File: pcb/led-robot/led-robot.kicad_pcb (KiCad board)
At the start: 2 copper layers, 29.2 x 26.2 mm, 30 parts, among them J1 data, U1 MAX7219

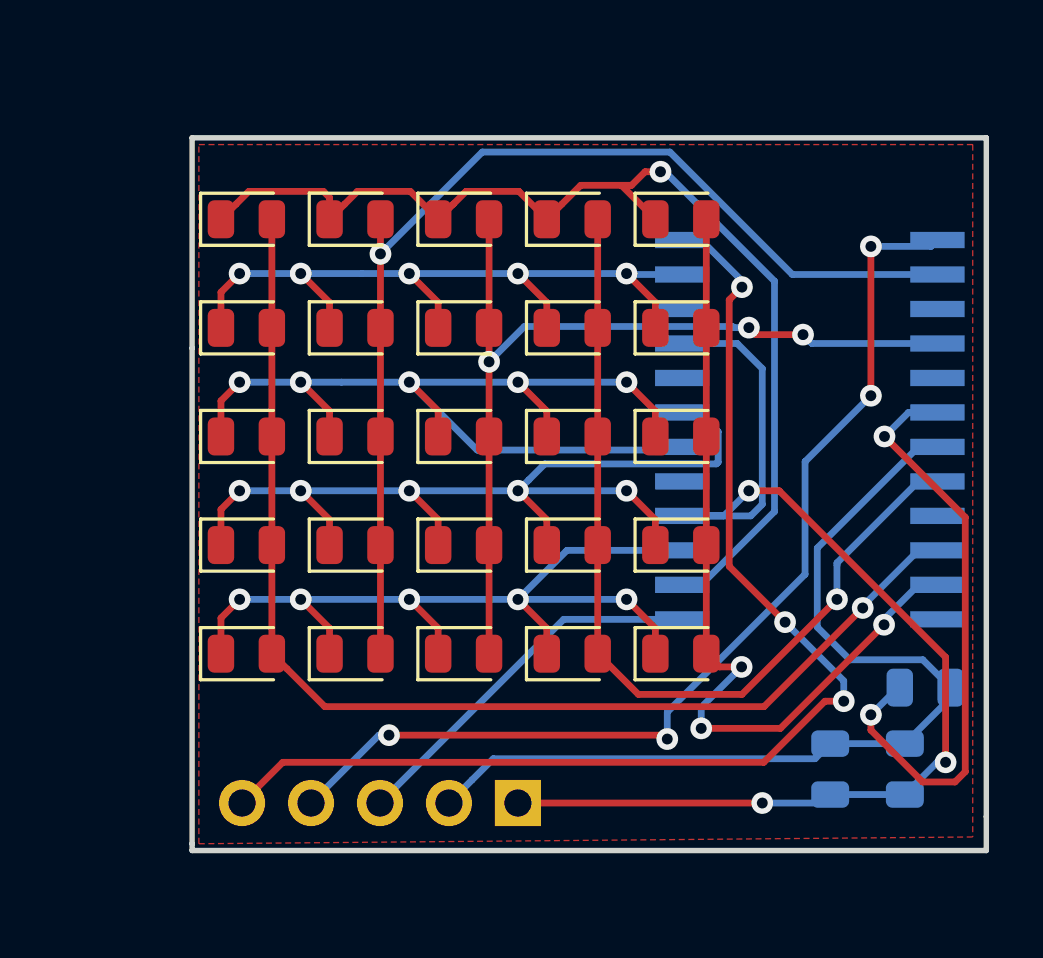
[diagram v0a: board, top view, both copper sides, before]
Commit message: update size
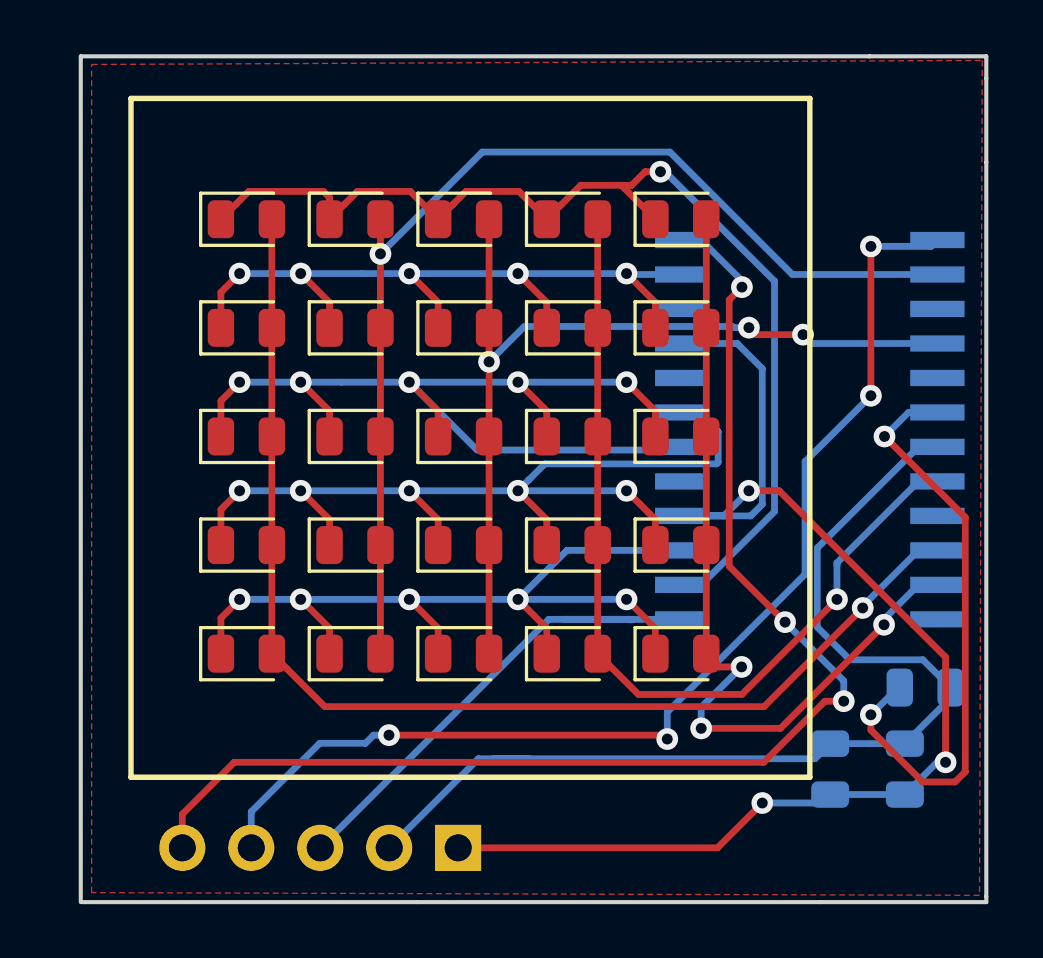
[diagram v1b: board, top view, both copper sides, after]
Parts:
- moved J1 2.75 mm to (190.8, 100.2)
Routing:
- net /DIN: track 13.9 -> 19.4 mm
- net +5V: track 35.2 -> 39.4 mm
- net /CLK: track 38.0 -> 42.0 mm
- net /LOAD: track 44.0 -> 47.6 mm
- net GND: track 44.3 -> 47.2 mm
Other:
- board size 29.2 x 26.2 mm -> 33.3 x 31.2 mm
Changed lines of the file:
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@@
   (general
     (thickness 1.6)
-    (drawings 12)
-    (tracks 247)
+    (drawings 19)
+    (tracks 256)
     (zones 0)
     (modules 30)
@@
   )
   (module Connector_PinHeader_2.54mm:PinHeader_1x05_P2.54mm_Vertical (layer B.Cu)
-    (at 193 98.5 90)
+    (at 190.8 100.15 90)
     (descr "Through hole straight pin header, 1x05, 2.54mm pitch, single row")
     (tags "Through hole pin header THT 1x05 2.54mm single row")
@@
     )
   )
+  (gr_line (start 210.25 101.95) (end 210.25 102.15) (layer Edge.Cuts) (width 0.15))
+  (gr_line (start 210.25 74.9) (end 210.25 101.95) (layer Edge.Cuts) (width 0.15))
+  (gr_line (start 210.25 71.8) (end 210.25 74.9) (layer Edge.Cuts) (width 0.15))
+  (gr_line (start 210.25 71) (end 210.25 71.8) (layer Edge.Cuts) (width 0.15))
+  (gr_line (start 204.15 102.15) (end 210.25 102.15) (layer Edge.Cuts) (width 0.15))
+  (gr_line (start 189.3 102.15) (end 204.15 102.15) (layer Edge.Cuts) (width 0.15))
+  (gr_line (start 176.95 102.15) (end 189.3 102.15) (layer Edge.Cuts) (width 0.15))
+  (gr_line (start 176.9 71) (end 176.9 102.15) (layer Edge.Cuts) (width 0.15))
+  (gr_line (start 205.95 71) (end 176.9 71) (layer Edge.Cuts) (width 0.15))
+  (gr_line (start 210.25 71) (end 205.95 71) (layer Edge.Cuts) (width 0.15))
+  (gr_line (start 203.75 97.55) (end 203.75 72.55) (layer F.SilkS) (width 0.2))
+  (gr_line (start 178.75 97.55) (end 203.75 97.55) (layer F.SilkS) (width 0.2))
+  (gr_line (start 178.75 97.55) (end 178.75 72.55) (layer F.SilkS) (width 0.2))
+  (gr_line (start 178.75 72.55) (end 203.75 72.55) (layer F.SilkS) (width 0.2))
   (gr_text GND (at 193.25 94.25 270) (layer B.SilkS)
     (effects (font (size 1.5 1.5) (thickness 0.3)) (justify mirror))
@@
     (effects (font (size 1.5 1.5) (thickness 0.3)) (justify mirror))
   )
-  (gr_line (start 181 100.25) (end 181 100) (layer Edge.Cuts) (width 0.2))
-  (gr_line (start 210.25 100.25) (end 181 100.25) (layer Edge.Cuts) (width 0.2))
-  (gr_line (start 210.25 99) (end 210.25 100.25) (layer Edge.Cuts) (width 0.2))
-  (gr_line (start 210.25 74) (end 210.25 99) (layer Edge.Cuts) (width 0.2))
-  (gr_line (start 181 74) (end 210.25 74) (layer Edge.Cuts) (width 0.2))
-  (gr_line (start 181 81.75) (end 181 74) (layer Edge.Cuts) (width 0.2))
-  (gr_line (start 181 100) (end 181 81.75) (layer Edge.Cuts) (width 0.2))
   (via (at 197 87) (size 0.8) (drill 0.4) (layers F.Cu B.Cu) (net 1))
   (segment (start 198.0625 88.0625) (end 197 87) (width 0.25) (layer F.Cu) (net 1))
@@
   (segment (start 204.5 98.1875) (end 207.25 98.1875) (width 0.25) (layer B.Cu) (net 10))
   (via (at 202 98.5) (size 0.8) (drill 0.4) (layers F.Cu B.Cu) (net 10))
-  (segment (start 193 98.5) (end 202 98.5) (width 0.25) (layer F.Cu) (net 10))
   (segment (start 204.1875 98.5) (end 204.5 98.1875) (width 0.25) (layer B.Cu) (net 10))
   (segment (start 202 98.5) (end 204.1875 98.5) (width 0.25) (layer B.Cu) (net 10))
@@
   (segment (start 208.4375 97) (end 207.25 98.1875) (width 0.25) (layer B.Cu) (net 10))
   (segment (start 208.75 97) (end 208.4375 97) (width 0.25) (layer B.Cu) (net 10))
+  (segment (start 200.35 100.15) (end 202 98.5) (width 0.25) (layer F.Cu) (net 10))
+  (segment (start 190.8 100.15) (end 200.35 100.15) (width 0.25) (layer F.Cu) (net 10))
   (via (at 206 95.25) (size 0.8) (drill 0.4) (layers F.Cu B.Cu) (net 11))
   (segment (start 207 94.25) (end 206 95.25) (width 0.25) (layer B.Cu) (net 11))
@@
   (segment (start 207.25 96.3125) (end 208.9375 94.625) (width 0.25) (layer B.Cu) (net 12))
   (segment (start 207.25 96.3125) (end 204.5 96.3125) (width 0.25) (layer B.Cu) (net 12))
-  (segment (start 191.309999 97.650001) (end 190.46 98.5) (width 0.25) (layer B.Cu) (net 12))
-  (segment (start 192.091263 96.868737) (end 191.309999 97.650001) (width 0.25) (layer B.Cu) (net 12))
-  (segment (start 203.943763 96.868737) (end 192.091263 96.868737) (width 0.25) (layer B.Cu) (net 12))
   (segment (start 204.5 96.3125) (end 203.943763 96.868737) (width 0.25) (layer B.Cu) (net 12))
+  (segment (start 191.541263 96.868737) (end 193.4 96.868737) (width 0.25) (layer B.Cu) (net 12))
+  (segment (start 188.26 100.15) (end 191.541263 96.868737) (width 0.25) (layer B.Cu) (net 12))
+  (segment (start 193.4 96.868737) (end 192.091263 96.868737) (width 0.25) (layer B.Cu) (net 12))
+  (segment (start 203.943763 96.868737) (end 193.4 96.868737) (width 0.25) (layer B.Cu) (net 12))
   (segment (start 183.9375 77) (end 183.9375 93) (width 0.25) (layer F.Cu) (net 13))
   (via (at 205.698685 91.316228) (size 0.8) (drill 0.4) (layers F.Cu B.Cu) (net 13))
@@
   (segment (start 185.88751 94.95001) (end 184.493737 93.556237) (width 0.25) (layer F.Cu) (net 13))
   (segment (start 205.698685 91.316228) (end 202.064903 94.95001) (width 0.25) (layer F.Cu) (net 13))
-  (segment (start 194.685 91.735) (end 199.05 91.735) (width 0.25) (layer B.Cu) (net 21))
-  (segment (start 187.92 98.5) (end 194.685 91.735) (width 0.25) (layer B.Cu) (net 21))
+  (segment (start 185.72 100.15) (end 194.135 91.735) (width 0.25) (layer B.Cu) (net 21))
+  (segment (start 197.25 91.735) (end 199.05 91.735) (width 0.25) (layer B.Cu) (net 21))
+  (segment (start 194.135 91.735) (end 197.25 91.735) (width 0.25) (layer B.Cu) (net 21))
+  (segment (start 194.685 91.735) (end 197.25 91.735) (width 0.25) (layer B.Cu) (net 21))
   (via (at 188.25 96) (size 0.8) (drill 0.4) (layers F.Cu B.Cu) (net 22))
   (segment (start 187.88 96) (end 188.25 96) (width 0.25) (layer B.Cu) (net 22))
-  (segment (start 185.38 98.5) (end 187.88 96) (width 0.25) (layer B.Cu) (net 22))
   (segment (start 198.356263 96) (end 198.5 96.143737) (width 0.25) (layer F.Cu) (net 22))
   (via (at 198.5 96.143737) (size 0.8) (drill 0.4) (layers F.Cu B.Cu) (net 22))
@@
   (segment (start 208.215 78) (end 208.45 77.765) (width 0.25) (layer B.Cu) (net 22))
   (segment (start 206 78) (end 208.215 78) (width 0.25) (layer B.Cu) (net 22))
+  (segment (start 187.684315 96) (end 187.384315 96.3) (width 0.25) (layer B.Cu) (net 22))
+  (segment (start 188.25 96) (end 187.684315 96) (width 0.25) (layer B.Cu) (net 22))
+  (segment (start 187.384315 96.3) (end 185.7 96.3) (width 0.25) (layer B.Cu) (net 22))
+  (segment (start 183.18 98.82) (end 183.18 100.15) (width 0.25) (layer B.Cu) (net 22))
+  (segment (start 185.7 96.3) (end 183.18 98.82) (width 0.25) (layer B.Cu) (net 22))
   (via (at 201.25 79.5) (size 0.8) (drill 0.4) (layers F.Cu B.Cu) (net 23))
   (segment (start 201.25 79.265) (end 201.25 79.5) (width 0.25) (layer B.Cu) (net 23))
@@
   (segment (start 205 94) (end 205 94.75) (width 0.25) (layer B.Cu) (net 23))
   (segment (start 202.838499 91.838499) (end 205 94) (width 0.25) (layer B.Cu) (net 23))
+  (segment (start 180.64 98.91) (end 180.64 100.15) (width 0.25) (layer F.Cu) (net 23))
   (segment (start 204.305578 94.75) (end 202.055578 97) (width 0.25) (layer F.Cu) (net 23))
+  (segment (start 202.055578 97) (end 182.55 97) (width 0.25) (layer F.Cu) (net 23))
   (segment (start 205 94.75) (end 204.305578 94.75) (width 0.25) (layer F.Cu) (net 23))
-  (segment (start 184.34 97) (end 182.84 98.5) (width 0.25) (layer F.Cu) (net 23))
-  (segment (start 202.055578 97) (end 184.34 97) (width 0.25) (layer F.Cu) (net 23))
+  (segment (start 182.55 97) (end 180.64 98.91) (width 0.25) (layer F.Cu) (net 23))
   (zone (net 10) (net_name GND) (layer F.Cu) (hatch edge 0.508)
     (connect_pads (clearance 0.508))
@@
     (polygon
       (pts
-        (xy 181.25 74.25) (xy 209.75 74.25) (xy 209.75 99.75) (xy 181.25 100)
+        (xy 177.3 71.3) (xy 210.1 71.15) (xy 210 101.9) (xy 177.3 101.8)
       )
     )

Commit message: update pcb to fit spacing inside MDF
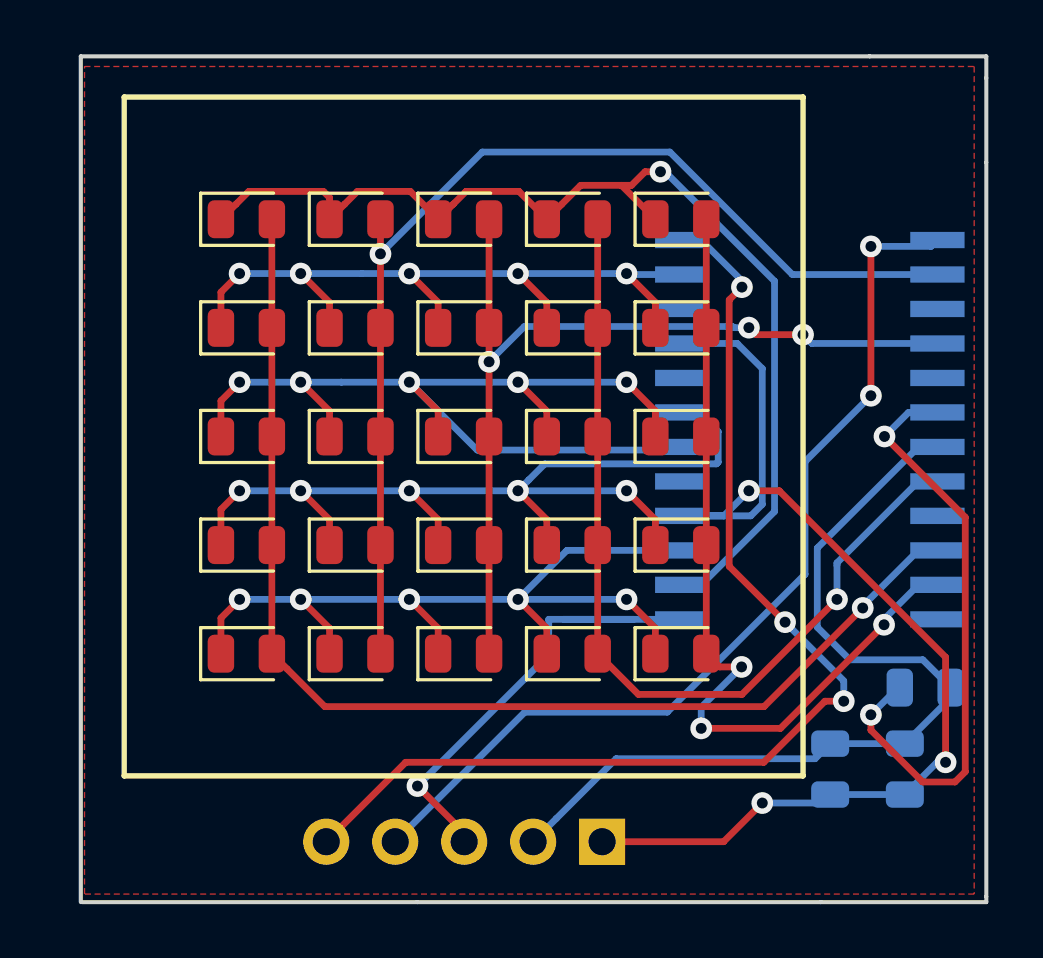
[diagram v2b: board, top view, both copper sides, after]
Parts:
- moved J1 5.30 mm to (196.1, 99.9)
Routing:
- net /CLK: track 42.0 -> 34.8 mm, vias 4 -> 2
- net +5V: track 39.4 -> 32.7 mm
- net /LOAD: track 47.6 -> 41.5 mm
- net GND: track 47.2 -> 41.8 mm
- net /DIN: track 19.4 -> 18.4 mm, vias 0 -> 1
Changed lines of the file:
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@@
     (thickness 1.6)
     (drawings 19)
-    (tracks 256)
+    (tracks 249)
     (zones 0)
     (modules 30)
@@
       (usegerberadvancedattributes false)
       (creategerberjobfile false)
-      (excludeedgelayer true)
+      (excludeedgelayer false)
       (linewidth 0.100000)
       (plotframeref false)
@@
       (plotvalue true)
       (plotinvisibletext false)
-      (padsonsilk false)
+      (padsonsilk true)
       (subtractmaskfromsilk false)
       (outputformat 1)
@@
   )
   (module Connector_PinHeader_2.54mm:PinHeader_1x05_P2.54mm_Vertical (layer B.Cu)
-    (at 190.8 100.15 90)
+    (at 196.1 99.925 90)
     (descr "Through hole straight pin header, 1x05, 2.54mm pitch, single row")
     (tags "Through hole pin header THT 1x05 2.54mm single row")
@@
   (gr_line (start 205.95 71) (end 176.9 71) (layer Edge.Cuts) (width 0.15))
   (gr_line (start 210.25 71) (end 205.95 71) (layer Edge.Cuts) (width 0.15))
-  (gr_line (start 203.75 97.55) (end 203.75 72.55) (layer F.SilkS) (width 0.2))
-  (gr_line (start 178.75 97.55) (end 203.75 97.55) (layer F.SilkS) (width 0.2))
-  (gr_line (start 178.75 97.55) (end 178.75 72.55) (layer F.SilkS) (width 0.2))
-  (gr_line (start 178.75 72.55) (end 203.75 72.55) (layer F.SilkS) (width 0.2))
-  (gr_text GND (at 193.25 94.25 270) (layer B.SilkS)
+  (gr_line (start 203.5 97.5) (end 203.5 72.5) (layer F.SilkS) (width 0.2))
+  (gr_line (start 178.5 97.5) (end 203.5 97.5) (layer F.SilkS) (width 0.2))
+  (gr_line (start 178.5 97.5) (end 178.5 72.5) (layer F.SilkS) (width 0.2))
+  (gr_line (start 178.5 72.5) (end 203.5 72.5) (layer F.SilkS) (width 0.2))
+  (gr_text GND (at 196.088 95.758 270) (layer B.SilkS)
     (effects (font (size 1.5 1.5) (thickness 0.3)) (justify mirror))
   )
-  (gr_text 5V (at 190.5 95 270) (layer B.SilkS)
+  (gr_text 5V (at 193.294 96.52 270) (layer B.SilkS)
     (effects (font (size 1.5 1.5) (thickness 0.3)) (justify mirror))
   )
-  (gr_text DIN (at 188 94.5 270) (layer B.SilkS)
+  (gr_text DIN (at 190.754 96.012 270) (layer B.SilkS)
     (effects (font (size 1.5 1.5) (thickness 0.3)) (justify mirror))
   )
-  (gr_text CLK (at 185.25 94.5 270) (layer B.SilkS)
+  (gr_text CLK (at 188.214 95.758 270) (layer B.SilkS)
     (effects (font (size 1.5 1.5) (thickness 0.3)) (justify mirror))
   )
-  (gr_text LOAD (at 182.75 93.75 270) (layer B.SilkS)
+  (gr_text LOAD (at 185.928 94.996 270) (layer B.SilkS)
     (effects (font (size 1.5 1.5) (thickness 0.3)) (justify mirror))
   )
@@
   (segment (start 208.4375 97) (end 207.25 98.1875) (width 0.25) (layer B.Cu) (net 10))
   (segment (start 208.75 97) (end 208.4375 97) (width 0.25) (layer B.Cu) (net 10))
-  (segment (start 200.35 100.15) (end 202 98.5) (width 0.25) (layer F.Cu) (net 10))
-  (segment (start 190.8 100.15) (end 200.35 100.15) (width 0.25) (layer F.Cu) (net 10))
+  (segment (start 200.575 99.925) (end 196.1 99.925) (width 0.25) (layer F.Cu) (net 10))
+  (segment (start 202 98.5) (end 200.575 99.925) (width 0.25) (layer F.Cu) (net 10))
   (via (at 206 95.25) (size 0.8) (drill 0.4) (layers F.Cu B.Cu) (net 11))
   (segment (start 207 94.25) (end 206 95.25) (width 0.25) (layer B.Cu) (net 11))
@@
   (segment (start 207.25 96.3125) (end 208.9375 94.625) (width 0.25) (layer B.Cu) (net 12))
   (segment (start 207.25 96.3125) (end 204.5 96.3125) (width 0.25) (layer B.Cu) (net 12))
+  (segment (start 196.616263 96.868737) (end 194.409999 99.075001) (width 0.25) (layer B.Cu) (net 12))
+  (segment (start 203.943763 96.868737) (end 196.616263 96.868737) (width 0.25) (layer B.Cu) (net 12))
+  (segment (start 194.409999 99.075001) (end 193.56 99.925) (width 0.25) (layer B.Cu) (net 12))
   (segment (start 204.5 96.3125) (end 203.943763 96.868737) (width 0.25) (layer B.Cu) (net 12))
-  (segment (start 191.541263 96.868737) (end 193.4 96.868737) (width 0.25) (layer B.Cu) (net 12))
-  (segment (start 188.26 100.15) (end 191.541263 96.868737) (width 0.25) (layer B.Cu) (net 12))
-  (segment (start 193.4 96.868737) (end 192.091263 96.868737) (width 0.25) (layer B.Cu) (net 12))
-  (segment (start 203.943763 96.868737) (end 193.4 96.868737) (width 0.25) (layer B.Cu) (net 12))
   (segment (start 183.9375 77) (end 183.9375 93) (width 0.25) (layer F.Cu) (net 13))
   (via (at 205.698685 91.316228) (size 0.8) (drill 0.4) (layers F.Cu B.Cu) (net 13))
@@
   (segment (start 185.88751 94.95001) (end 184.493737 93.556237) (width 0.25) (layer F.Cu) (net 13))
   (segment (start 205.698685 91.316228) (end 202.064903 94.95001) (width 0.25) (layer F.Cu) (net 13))
-  (segment (start 185.72 100.15) (end 194.135 91.735) (width 0.25) (layer B.Cu) (net 21))
   (segment (start 197.25 91.735) (end 199.05 91.735) (width 0.25) (layer B.Cu) (net 21))
   (segment (start 194.135 91.735) (end 197.25 91.735) (width 0.25) (layer B.Cu) (net 21))
   (segment (start 194.685 91.735) (end 197.25 91.735) (width 0.25) (layer B.Cu) (net 21))
-  (via (at 188.25 96) (size 0.8) (drill 0.4) (layers F.Cu B.Cu) (net 22))
-  (segment (start 187.88 96) (end 188.25 96) (width 0.25) (layer B.Cu) (net 22))
-  (segment (start 198.356263 96) (end 198.5 96.143737) (width 0.25) (layer F.Cu) (net 22))
-  (via (at 198.5 96.143737) (size 0.8) (drill 0.4) (layers F.Cu B.Cu) (net 22))
-  (segment (start 188.25 96) (end 198.356263 96) (width 0.25) (layer F.Cu) (net 22))
+  (via (at 189.3 97.875) (size 0.8) (drill 0.4) (layers F.Cu B.Cu) (net 21))
+  (segment (start 194.135 93.04) (end 189.3 97.875) (width 0.25) (layer B.Cu) (net 21))
+  (segment (start 194.135 91.735) (end 194.135 93.04) (width 0.25) (layer B.Cu) (net 21))
+  (segment (start 191.02 99.595) (end 191.02 99.925) (width 0.25) (layer F.Cu) (net 21))
+  (segment (start 189.3 97.875) (end 191.02 99.595) (width 0.25) (layer F.Cu) (net 21))
   (via (at 206 83.5) (size 0.8) (drill 0.4) (layers F.Cu B.Cu) (net 22))
-  (segment (start 198.5 96.143737) (end 198.5 95.151692) (width 0.25) (layer B.Cu) (net 22))
   (segment (start 203.57499 90.076702) (end 203.57499 85.92501) (width 0.25) (layer B.Cu) (net 22))
   (segment (start 198.5 95.151692) (end 203.57499 90.076702) (width 0.25) (layer B.Cu) (net 22))
@@
   (segment (start 208.215 78) (end 208.45 77.765) (width 0.25) (layer B.Cu) (net 22))
   (segment (start 206 78) (end 208.215 78) (width 0.25) (layer B.Cu) (net 22))
-  (segment (start 187.684315 96) (end 187.384315 96.3) (width 0.25) (layer B.Cu) (net 22))
-  (segment (start 188.25 96) (end 187.684315 96) (width 0.25) (layer B.Cu) (net 22))
-  (segment (start 187.384315 96.3) (end 185.7 96.3) (width 0.25) (layer B.Cu) (net 22))
-  (segment (start 183.18 98.82) (end 183.18 100.15) (width 0.25) (layer B.Cu) (net 22))
-  (segment (start 185.7 96.3) (end 183.18 98.82) (width 0.25) (layer B.Cu) (net 22))
+  (segment (start 193.253308 95.151692) (end 188.48 99.925) (width 0.25) (layer B.Cu) (net 22))
+  (segment (start 198.5 95.151692) (end 193.253308 95.151692) (width 0.25) (layer B.Cu) (net 22))
   (via (at 201.25 79.5) (size 0.8) (drill 0.4) (layers F.Cu B.Cu) (net 23))
   (segment (start 201.25 79.265) (end 201.25 79.5) (width 0.25) (layer B.Cu) (net 23))
@@
   (segment (start 205 94) (end 205 94.75) (width 0.25) (layer B.Cu) (net 23))
   (segment (start 202.838499 91.838499) (end 205 94) (width 0.25) (layer B.Cu) (net 23))
-  (segment (start 180.64 98.91) (end 180.64 100.15) (width 0.25) (layer F.Cu) (net 23))
   (segment (start 204.305578 94.75) (end 202.055578 97) (width 0.25) (layer F.Cu) (net 23))
-  (segment (start 202.055578 97) (end 182.55 97) (width 0.25) (layer F.Cu) (net 23))
   (segment (start 205 94.75) (end 204.305578 94.75) (width 0.25) (layer F.Cu) (net 23))
-  (segment (start 182.55 97) (end 180.64 98.91) (width 0.25) (layer F.Cu) (net 23))
+  (segment (start 188.865 97) (end 185.94 99.925) (width 0.25) (layer F.Cu) (net 23))
+  (segment (start 202.055578 97) (end 188.865 97) (width 0.25) (layer F.Cu) (net 23))
   (zone (net 10) (net_name GND) (layer F.Cu) (hatch edge 0.508)
     (connect_pads (clearance 0.508))
@@
     (polygon
       (pts
-        (xy 177.3 71.3) (xy 210.1 71.15) (xy 210 101.9) (xy 177.3 101.8)
+        (xy 209.804 71.374) (xy 209.804 101.854) (xy 177.038 101.854) (xy 177.038 71.374)
       )
     )
